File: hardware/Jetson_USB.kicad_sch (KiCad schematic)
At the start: 14 parts, among them U3 USBLC6-2SC6, U6 FT230XS

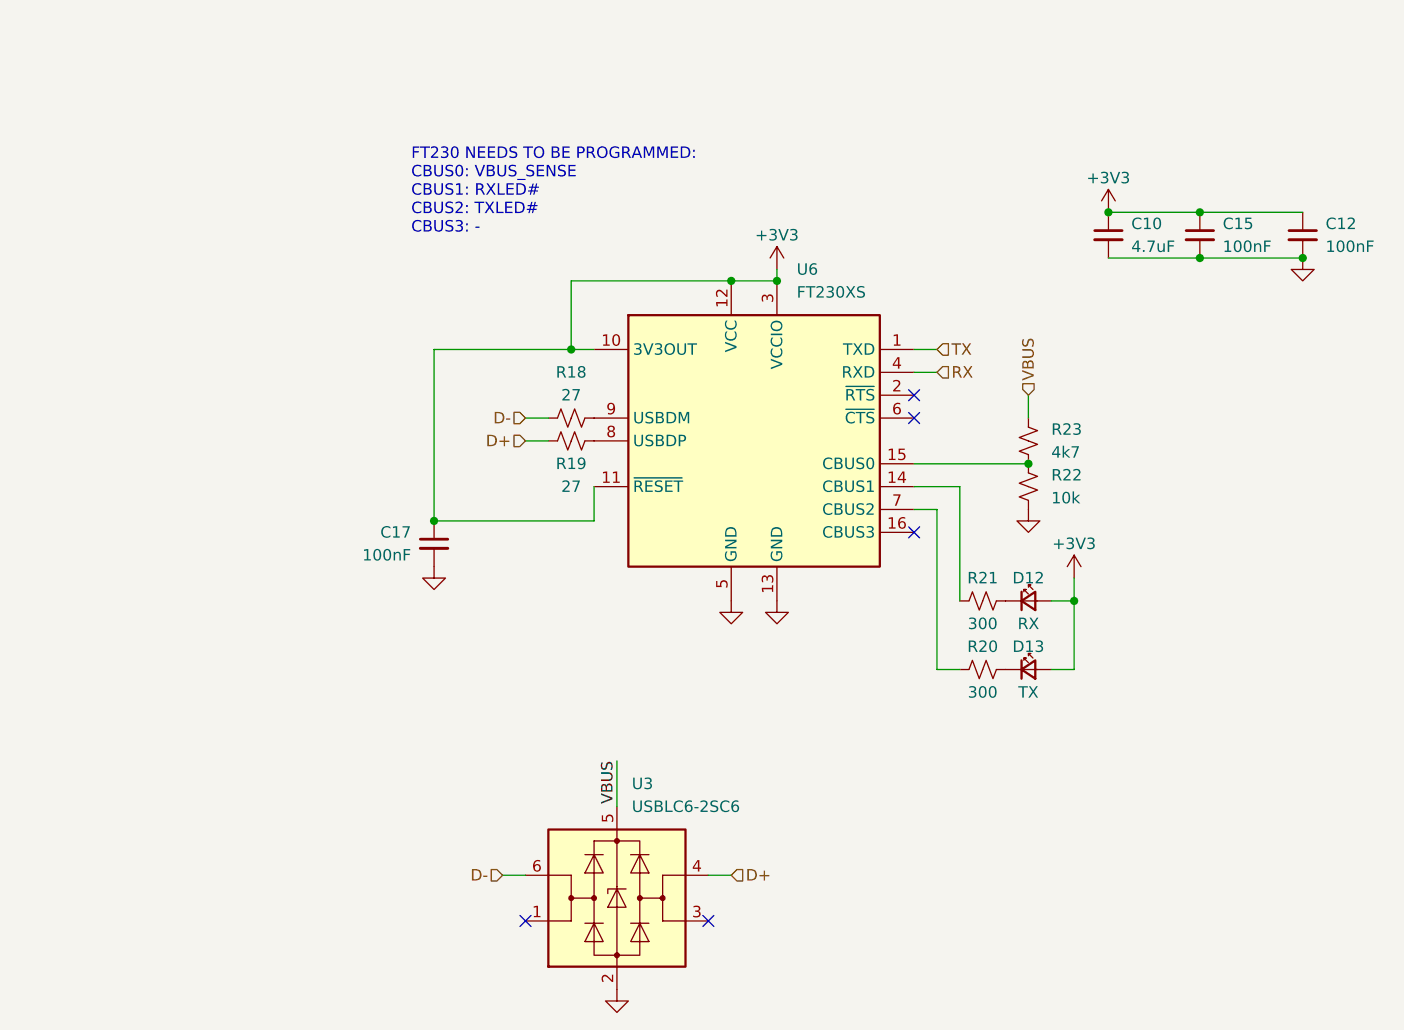
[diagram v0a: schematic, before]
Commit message: Isolate VCC from 3V3OUT, VDDIO, and nRESET (same as application example from datasheet)
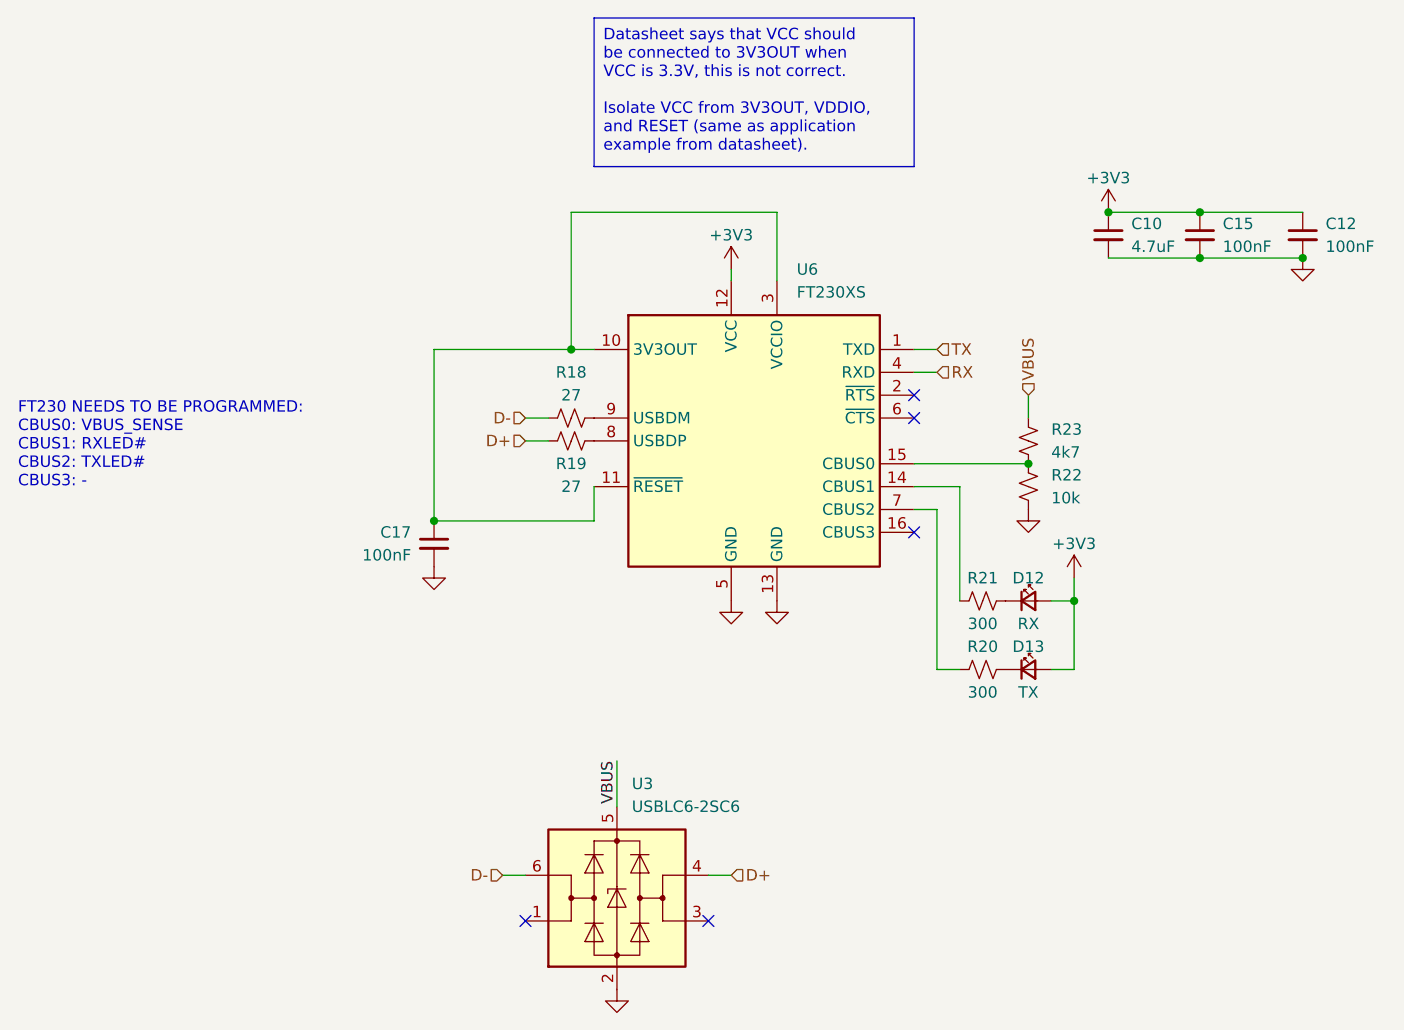
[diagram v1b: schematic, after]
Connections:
- net +3V3: no longer C17.1, U6.10 (3V3OUT), U6.11 (~{RESET}), U6.3 (VCCIO)
- new net: C17.1, U6.10 (3V3OUT), U6.11 (~{RESET}), U6.3 (VCCIO)
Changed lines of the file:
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@@
-	)
-	(junction
-		(at 156.21 71.12)
-		(diameter 0)
-		(color 0 0 0 0)
 	)
 	(junction
@@
 	(junction
 		(at 133.35 78.74)
-		(diameter 0)
-		(color 0 0 0 0)
-	)
-	(junction
-		(at 151.13 71.12)
 		(diameter 0)
 		(color 0 0 0 0)
@@
 	(wire
 		(pts
-			(xy 133.35 78.74) (xy 133.35 71.12)
-		)
-		(stroke
-			(width 0)
-			(type default)
-		)
-	)
-	(wire
-		(pts
 			(xy 171.45 96.52) (xy 173.99 96.52)
 		)
@@
 	(wire
 		(pts
+			(xy 151.13 69.85) (xy 151.13 71.12)
+		)
+		(stroke
+			(width 0)
+			(type default)
+		)
+	)
+	(wire
+		(pts
 			(xy 171.45 81.28) (xy 173.99 81.28)
 		)
@@
 	(wire
 		(pts
-			(xy 151.13 71.12) (xy 156.21 71.12)
+			(xy 133.35 63.5) (xy 133.35 78.74)
+		)
+		(stroke
+			(width 0)
+			(type default)
+		)
+	)
+	(wire
+		(pts
+			(xy 156.21 71.12) (xy 156.21 63.5)
 		)
 		(stroke
@@
 	(wire
 		(pts
-			(xy 133.35 71.12) (xy 151.13 71.12)
+			(xy 156.21 63.5) (xy 133.35 63.5)
 		)
 		(stroke
@@
 	(wire
 		(pts
-			(xy 156.21 69.85) (xy 156.21 71.12)
-		)
-		(stroke
-			(width 0)
-			(type default)
-		)
-	)
-	(wire
-		(pts
 			(xy 186.69 106.68) (xy 189.23 106.68)
 		)
@@
 			(width 0)
 			(type default)
+		)
+	)
+	(text_box "Datasheet says that VCC should be connected to 3V3OUT when VCC is 3.3V, this is not correct.\n\nIsolate VCC from 3V3OUT, VDDIO, and RESET (same as application example from datasheet)."
+		(exclude_from_sim no)
+		(at 135.89 41.91 0)
+		(size 35.56 16.51)
+		(stroke
+			(width 0)
+			(type default)
+		)
+		(fill
+			(type none)
+		)
+		(effects
+			(font
+				(size 1.27 1.27)
+			)
+			(justify left top)
 		)
 	)
 	(text "FT230 NEEDS TO BE PROGRAMMED:\nCBUS0: VBUS_SENSE\nCBUS1: RXLED#\nCBUS2: TXLED#\nCBUS3: -"
 		(exclude_from_sim no)
-		(at 115.57 66.04 0)
+		(at 71.882 94.234 0)
 		(effects
 			(font
@@
 	(symbol
 		(lib_id "power:+3V3")
-		(at 156.21 69.85 0)
+		(at 151.13 69.85 0)
 		(unit 1)
 		(exclude_from_sim no)
@@
 		(dnp no)
 		(property "Reference" "#PWR037"
-			(at 156.21 73.66 0)
+			(at 151.13 73.66 0)
 			(effects
 				(font
@@
 		)
 		(property "Value" "+3V3"
-			(at 156.21 66.04 0)
+			(at 151.13 66.04 0)
 			(effects
 				(font
@@
 		)
 		(property "Footprint" ""
-			(at 156.21 69.85 0)
+			(at 151.13 69.85 0)
 			(effects
 				(font
@@
 		)
 		(property "Datasheet" ""
-			(at 156.21 69.85 0)
+			(at 151.13 69.85 0)
 			(effects
 				(font
@@
 		)
 		(property "Description" ""
-			(at 156.21 69.85 0)
-			(effects
-				(font
+			(at 151.13 69.85 0)
+			(effects
+				(font

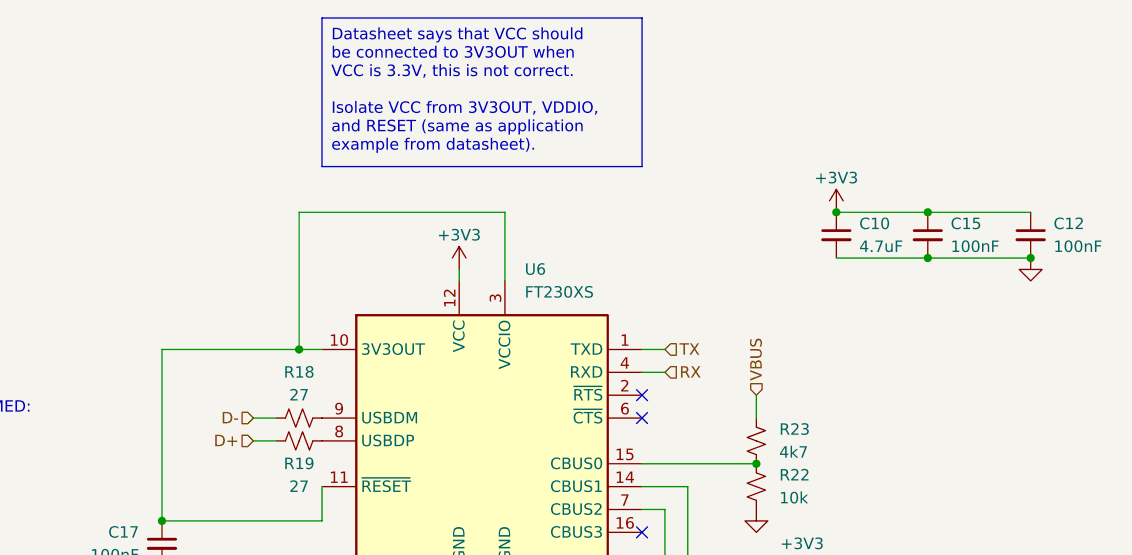
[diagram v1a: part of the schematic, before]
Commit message: Update PCB to reflect changes
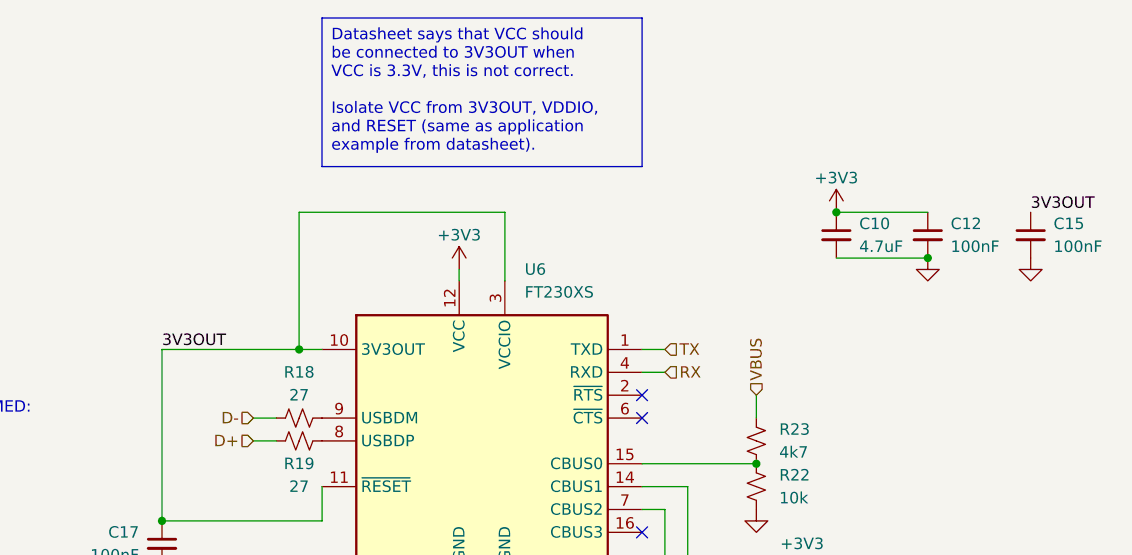
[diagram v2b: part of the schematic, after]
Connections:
- net +3V3: no longer C15.1
- net 3V3OUT: now reaches C17.1, U6.10 (3V3OUT), U6.11 (~{RESET}), U6.3 (VCCIO)
- net 3V3OUT: now also C15.1
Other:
- moved on the sheet: C12, C15
